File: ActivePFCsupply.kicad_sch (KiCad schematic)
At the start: 22 parts, among them Q1 IRF9540N, U1 LM358

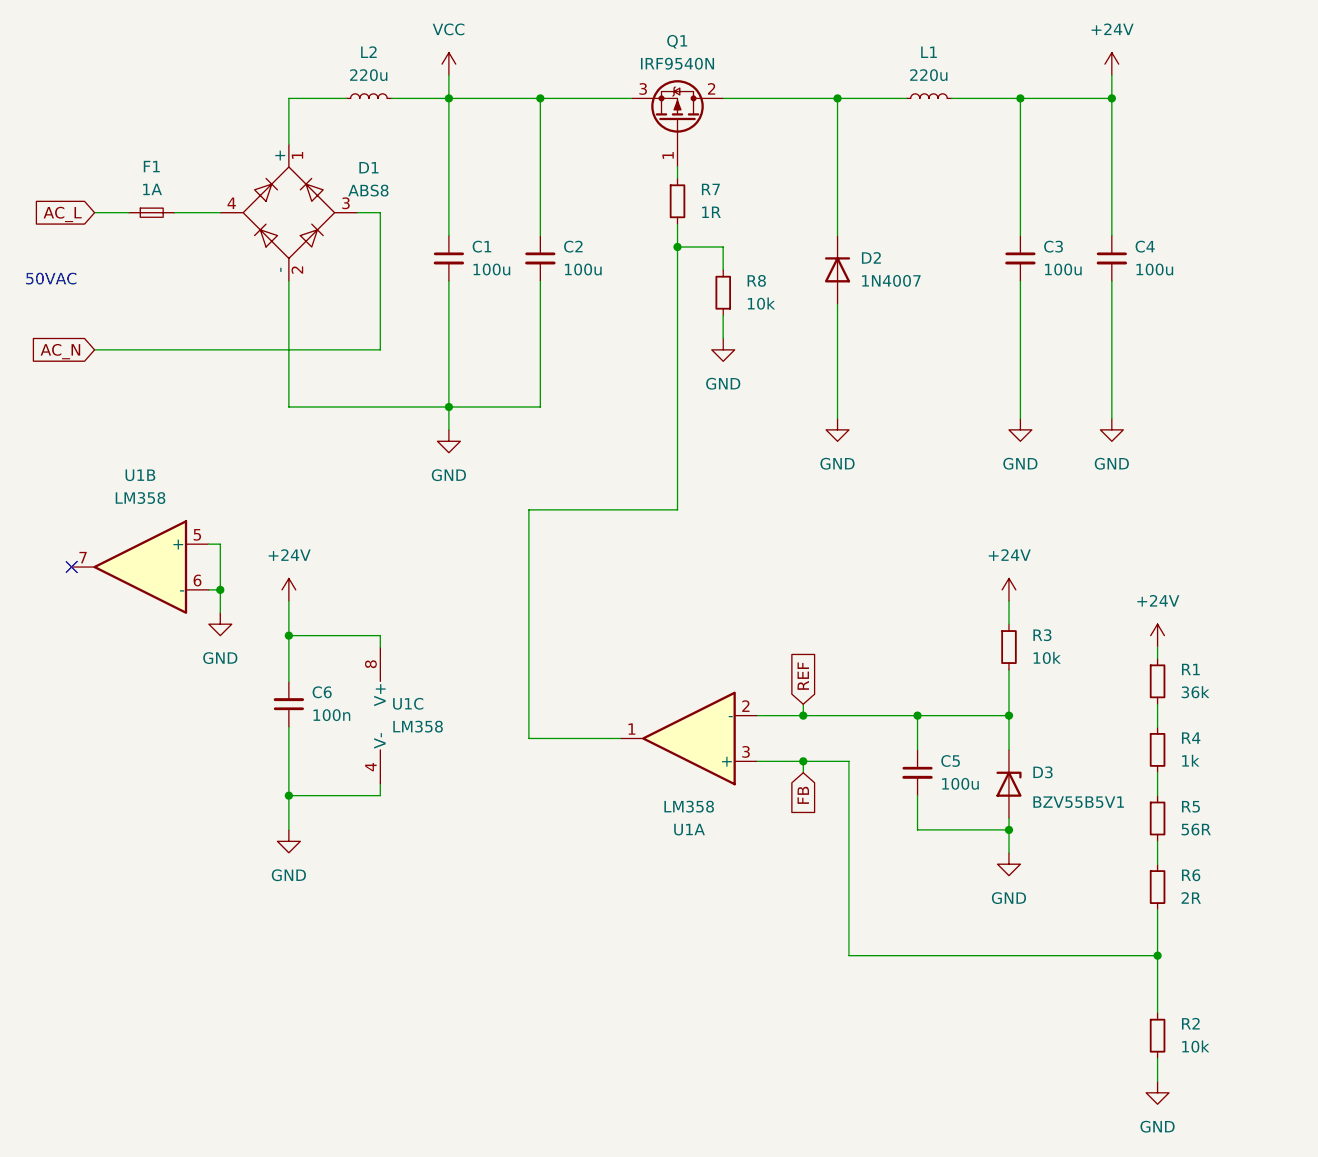
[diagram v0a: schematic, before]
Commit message: changed buck to boost topology.
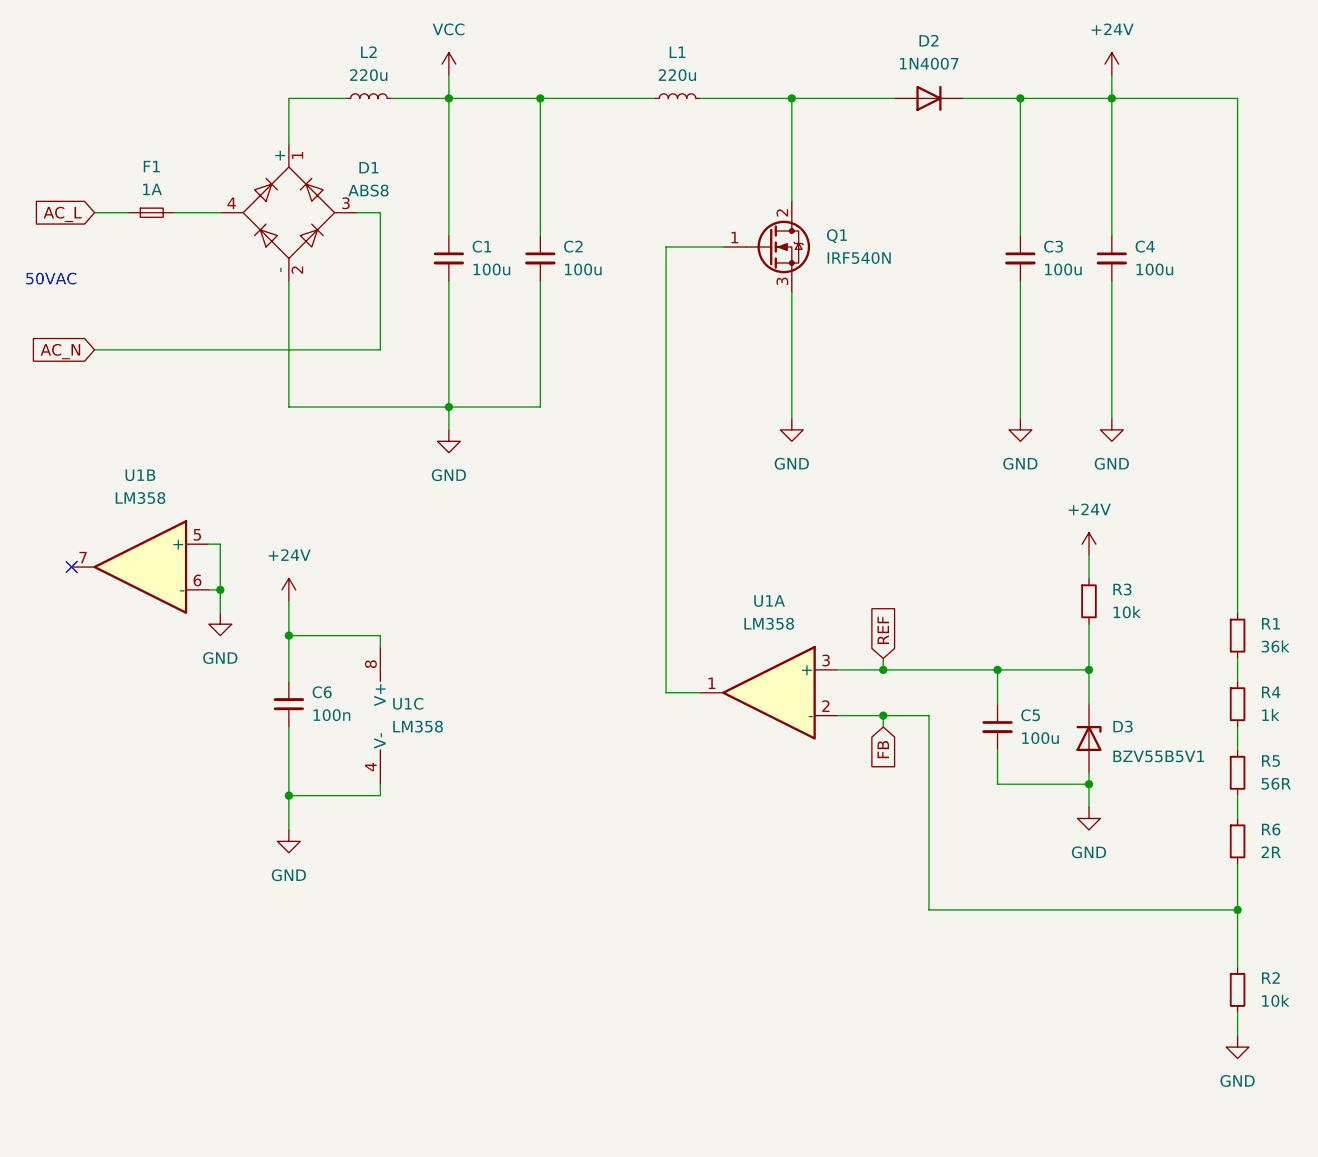
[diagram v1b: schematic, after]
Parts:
- removed Q1: IRF9540N, Package_TO_SOT_THT:TO-220-3_Vertical, symbol Transistor_FET:IRF9540N
- removed R7: 1R, Resistor_SMD:R_0603_1608Metric_Pad0.98x0.95mm_HandSolder, symbol Device:R_Small
- removed R8: 10k, Resistor_SMD:R_0603_1608Metric_Pad0.98x0.95mm_HandSolder, symbol Device:R_Small
- added Q1: IRF540N, Package_TO_SOT_THT:TO-220-3_Vertical, symbol Transistor_FET:IRF540N
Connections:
- net +24V: now also D2.1 (K); no longer L1.2
- net FB: now also U1.2 (-); no longer U1.3 (+)
- net GND: now also Q1.3 (S); no longer D2.2 (A)
- net REF: now also U1.3 (+); no longer U1.2 (-)
- net VCC: now also L1.1
- net at U1.1: now also Q1.1 (G)
- new net: D2.2 (A), L1.2, Q1.2 (D)
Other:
- moved on the sheet: C5, D3, R1, R2, R3, R4, R5, R6, U1A
